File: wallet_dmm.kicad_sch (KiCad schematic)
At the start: 6 parts, among them U1 TLC555xD

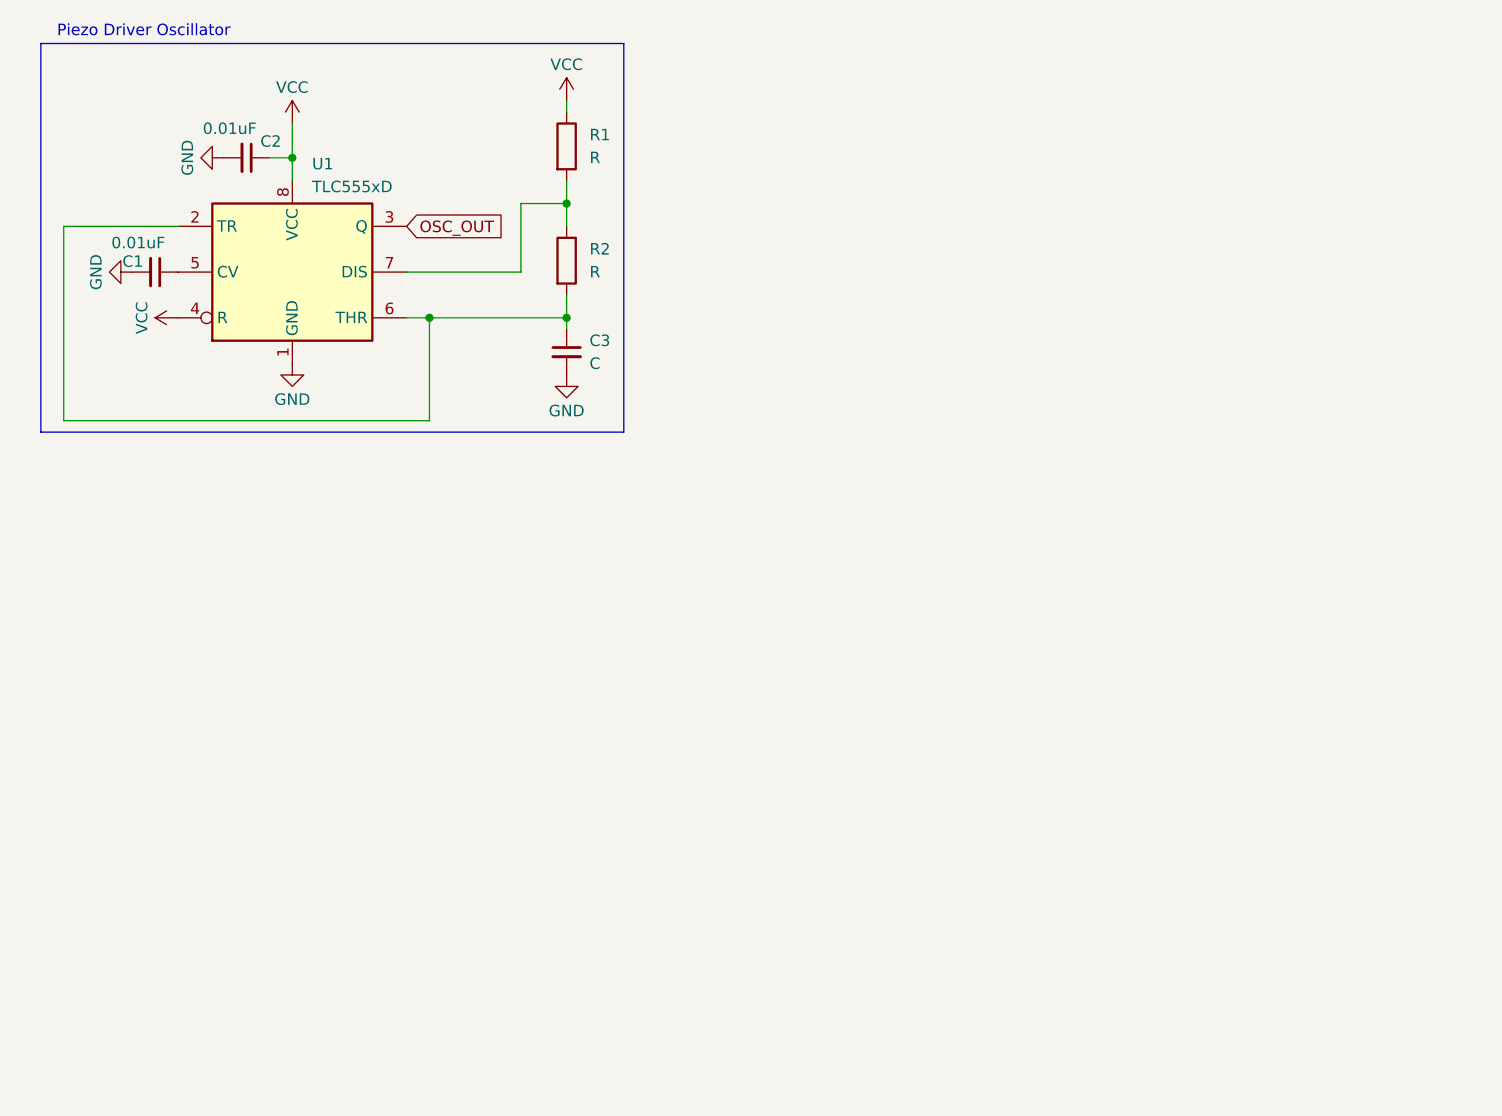
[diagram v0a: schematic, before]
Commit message: Merge pull request #5 from ArgonautGit/shane-working Added Oscillator Values
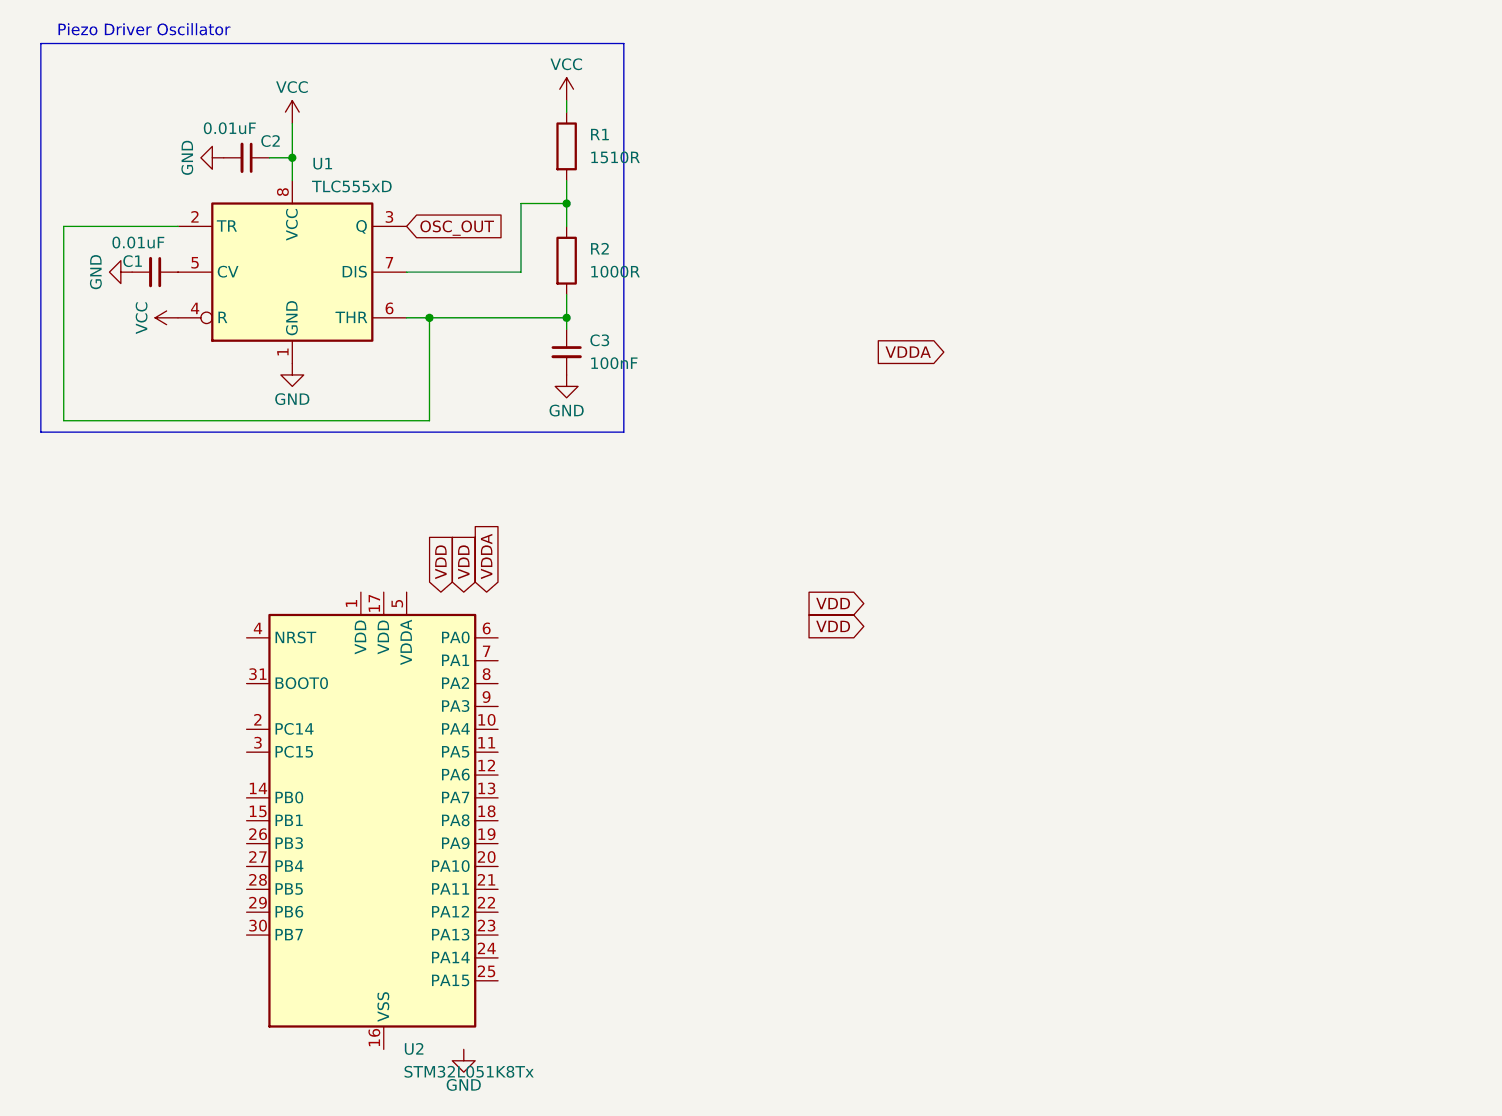
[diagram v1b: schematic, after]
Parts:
- added U2: STM32L051K8Tx, Package_QFP:LQFP-32_7x7mm_P0.8mm, symbol MCU_ST_STM32L0:STM32L051K8Tx
- C3: value C -> 100nF
- R1: value R -> 1510R
- R2: value R -> 1000R
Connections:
- new net: U2.16 (VSS), U2.32 (VSS)

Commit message: Merge pull request #6 from ArgonautGit/nick-working Pull request from my working branch.
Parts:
- added C4, C5, C6, C7, C8: 100nF, symbol Device:C_Small
- added J1: Conn_01x04, symbol Connector_Generic:Conn_01x04
- added JP1: BOOT0_JMP, Jumper:SolderJumper-2_P1.3mm_Open_RoundedPad1.0x1.5mm, symbol Jumper:Jumper_2_Open
- added R3: 1kR, symbol Device:R
- added SW1: REST_BUTTON, symbol Switch:SW_MEC_5G
- C2: value 0.01uF -> 10nF
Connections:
- net GND: now also U2.16 (VSS), U2.32 (VSS), C4.2, C5.2, C6.2, C7.2, C8.2, J1.4 (Pin_4), R3.2, SW1.3 (B), SW1.4 (B)
- net VCC: now also U2.1 (VDD), U2.17 (VDD), U2.5 (VDDA), C4.1, C5.1, C6.1, J1.3 (Pin_3), JP1.2 (B)
- net I2C1_SCL: now reaches U2.29 (PB6)
- net I2C1_SCL: now also J1.2 (Pin_2)
- net I2C1_SDA: now reaches U2.30 (PB7)
- net I2C1_SDA: now also J1.1 (Pin_1)
- net BOOT0: now reaches U2.31 (BOOT0)
- net BOOT0: now also C8.1, JP1.1 (A), R3.1
- net NRST: now reaches U2.4 (NRST)
- net NRST: now also C7.1, SW1.1 (A), SW1.2 (A)
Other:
- moved on the sheet: U2
